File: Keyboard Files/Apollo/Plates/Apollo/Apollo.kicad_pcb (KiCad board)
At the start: 2 copper layers, 315.1 x 130.2 mm, 62 parts

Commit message: Increase Apollo plate bezel
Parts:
- removed the REF** at (232.3, 167.5)
- removed the REF** at (311.7, 109.0)
- removed the REF** at (254.5, 111.4)
- removed the REF** at (330.7, 75.7)
- removed the REF** at (292.6, 125.7)
- removed the REF** at (248.3, 157.2)
- removed the REF** at (273.6, 109.0)
- removed the REF** at (330.7, 94.7)
- removed the REF** at (292.6, 106.7)
- removed the REF** at (292.6, 68.6)
- removed the REF** at (273.6, 70.9)
- removed the REF** at (330.7, 151.9)
- removed the REF** at (254.5, 73.3)
- removed the REF** at (330.7, 132.8)
- removed the REF** at (311.7, 128.1)
- removed the REF** at (273.6, 90.0)
- removed the REF** at (254.5, 130.5)
- removed the REF** at (311.7, 70.9)
- removed the REF** at (311.7, 147.1)
- removed the REF** at (292.6, 144.8)
- removed the REF** at (292.6, 87.6)
- removed the REF** at (273.6, 128.1)
- removed the REF** at (254.5, 92.4)
- removed the REF** at (311.7, 90.0)
- removed the REF** at (330.7, 113.8)
- removed the REF** at (271.7, 149.6)
- removed the REF** at (354.5, 113.8)
- removed the REF** at (354.5, 132.8)
- removed the REF** at (354.5, 75.7)
- removed the REF** at (354.5, 151.9)
- removed the REF** at (354.5, 94.7)
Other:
- board size 315.1 x 130.2 mm -> 164.5 x 133.6 mm

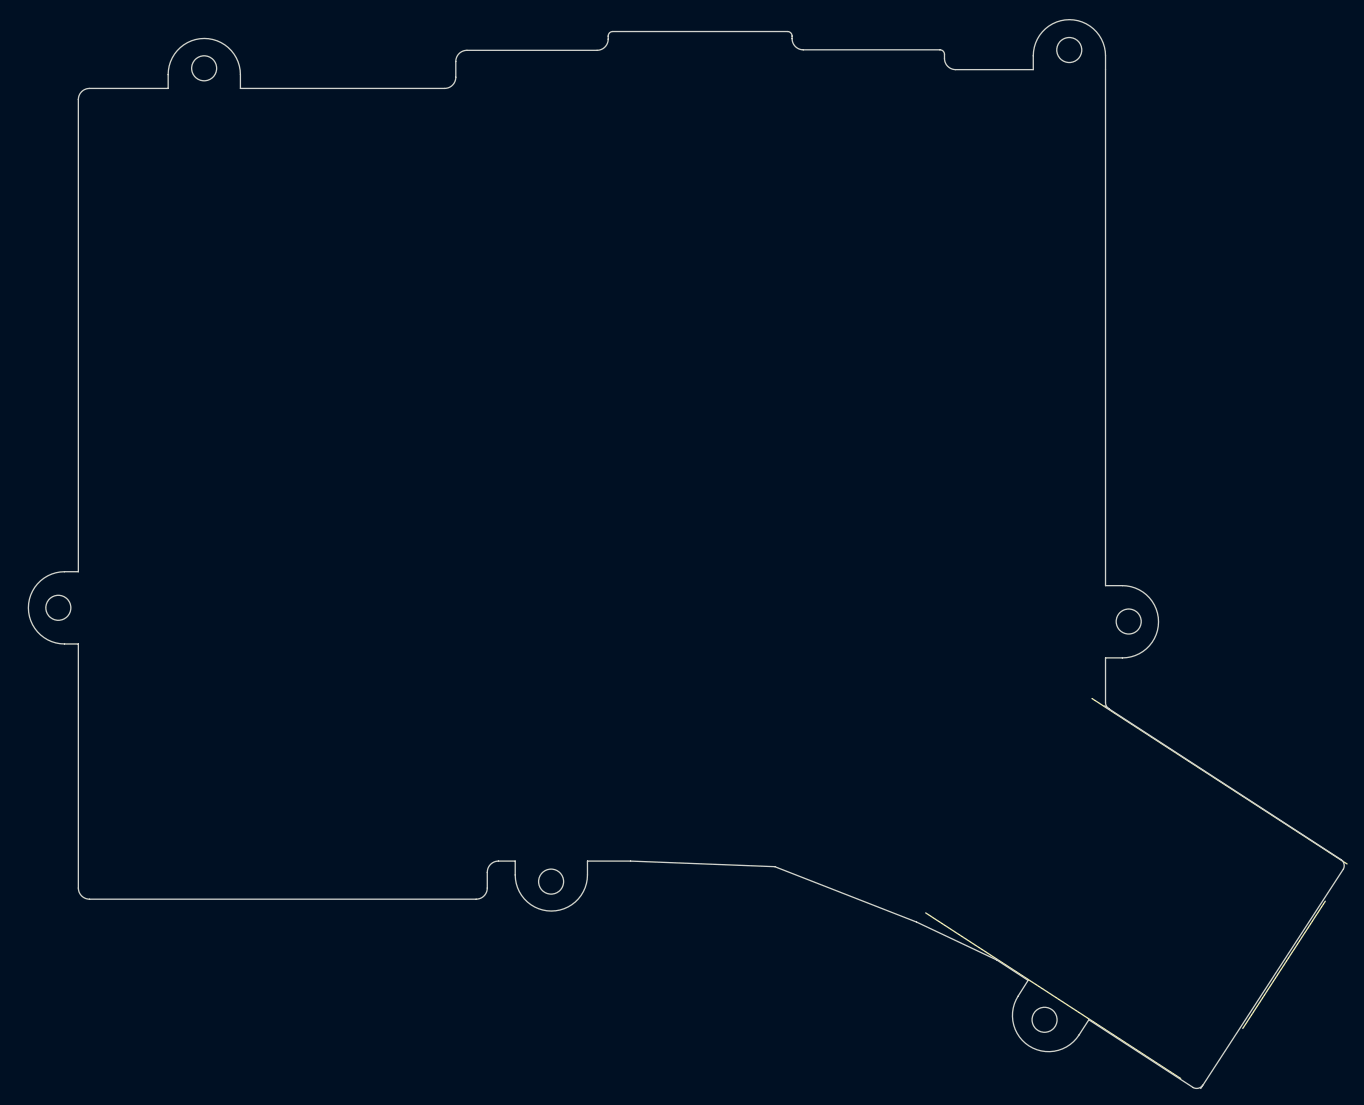
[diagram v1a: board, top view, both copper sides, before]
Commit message: Update Apollo plate for 1.5u
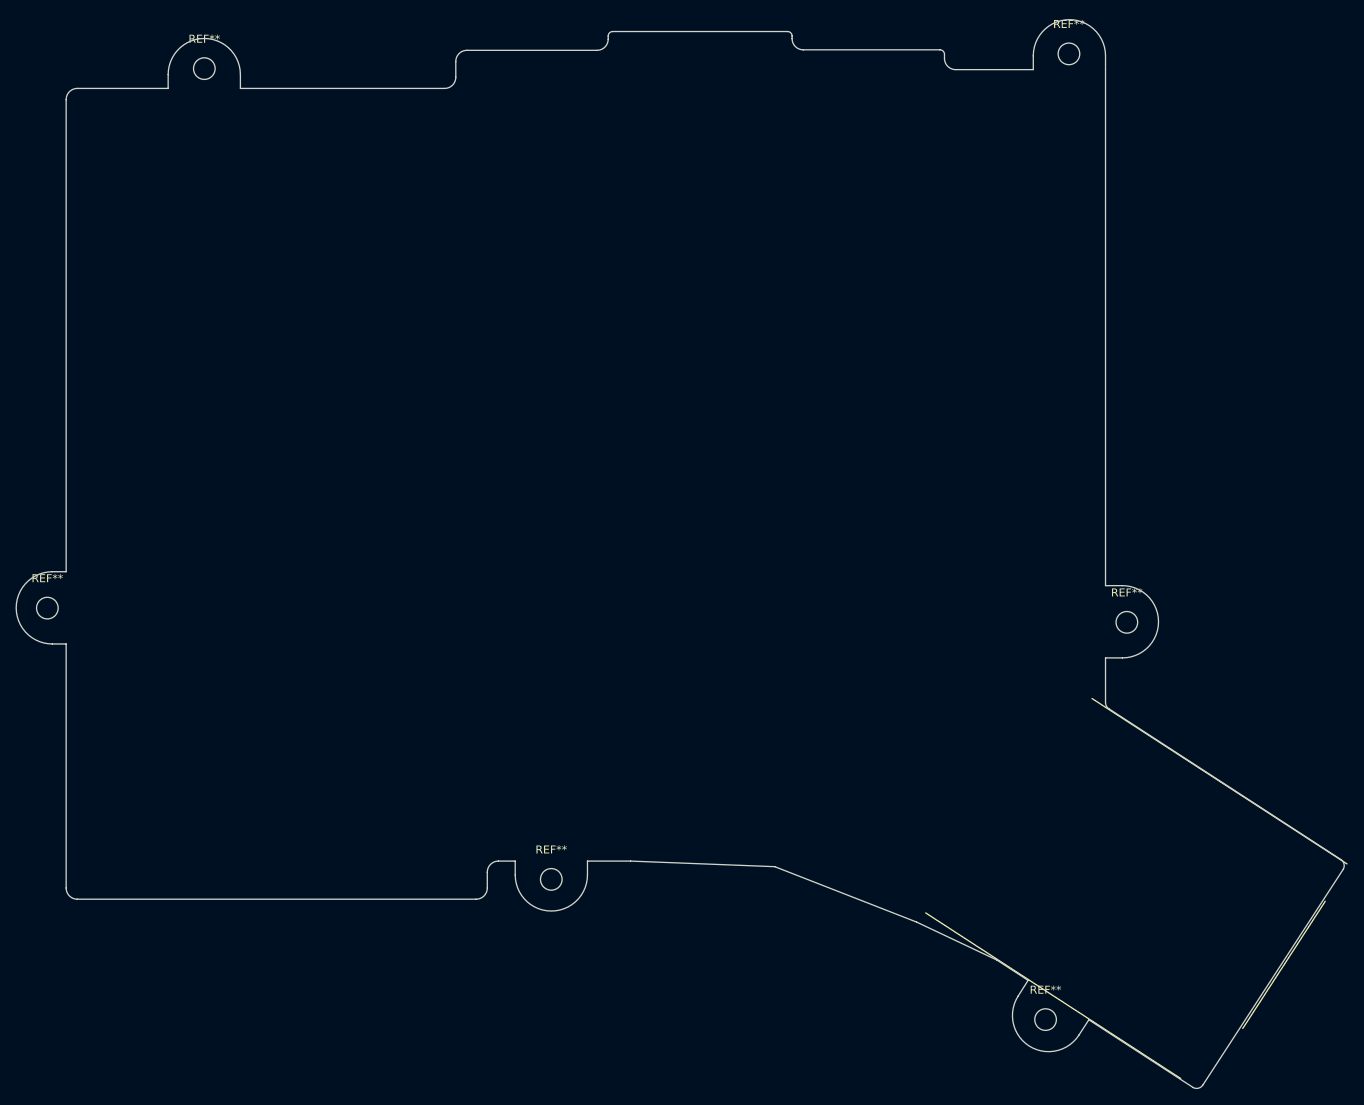
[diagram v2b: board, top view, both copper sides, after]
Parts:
- added REF**: MountingHole_2.7mm_M2.5, MountingHole:MountingHole_2.7mm_M2.5, F.Cu at (178.8, 179.5)
- added REF**: MountingHole_2.7mm_M2.5, MountingHole:MountingHole_2.7mm_M2.5, F.Cu at (188.9, 129.9)
- added REF**: MountingHole_2.7mm_M2.5, MountingHole:MountingHole_2.7mm_M2.5, F.Cu at (181.7, 58.8)
- added REF**: MountingHole_2.7mm_M2.5, MountingHole:MountingHole_2.7mm_M2.5, F.Cu at (73.6, 60.6)
- added REF**: MountingHole_2.7mm_M2.5, MountingHole:MountingHole_2.7mm_M2.5, F.Cu at (117.0, 162.0)
- added REF**: MountingHole_2.7mm_M2.5, MountingHole:MountingHole_2.7mm_M2.5, F.Cu at (54.0, 128.1)
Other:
- board size 164.5 x 133.6 mm -> 166 x 133.6 mm
